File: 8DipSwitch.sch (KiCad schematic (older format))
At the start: 12 parts

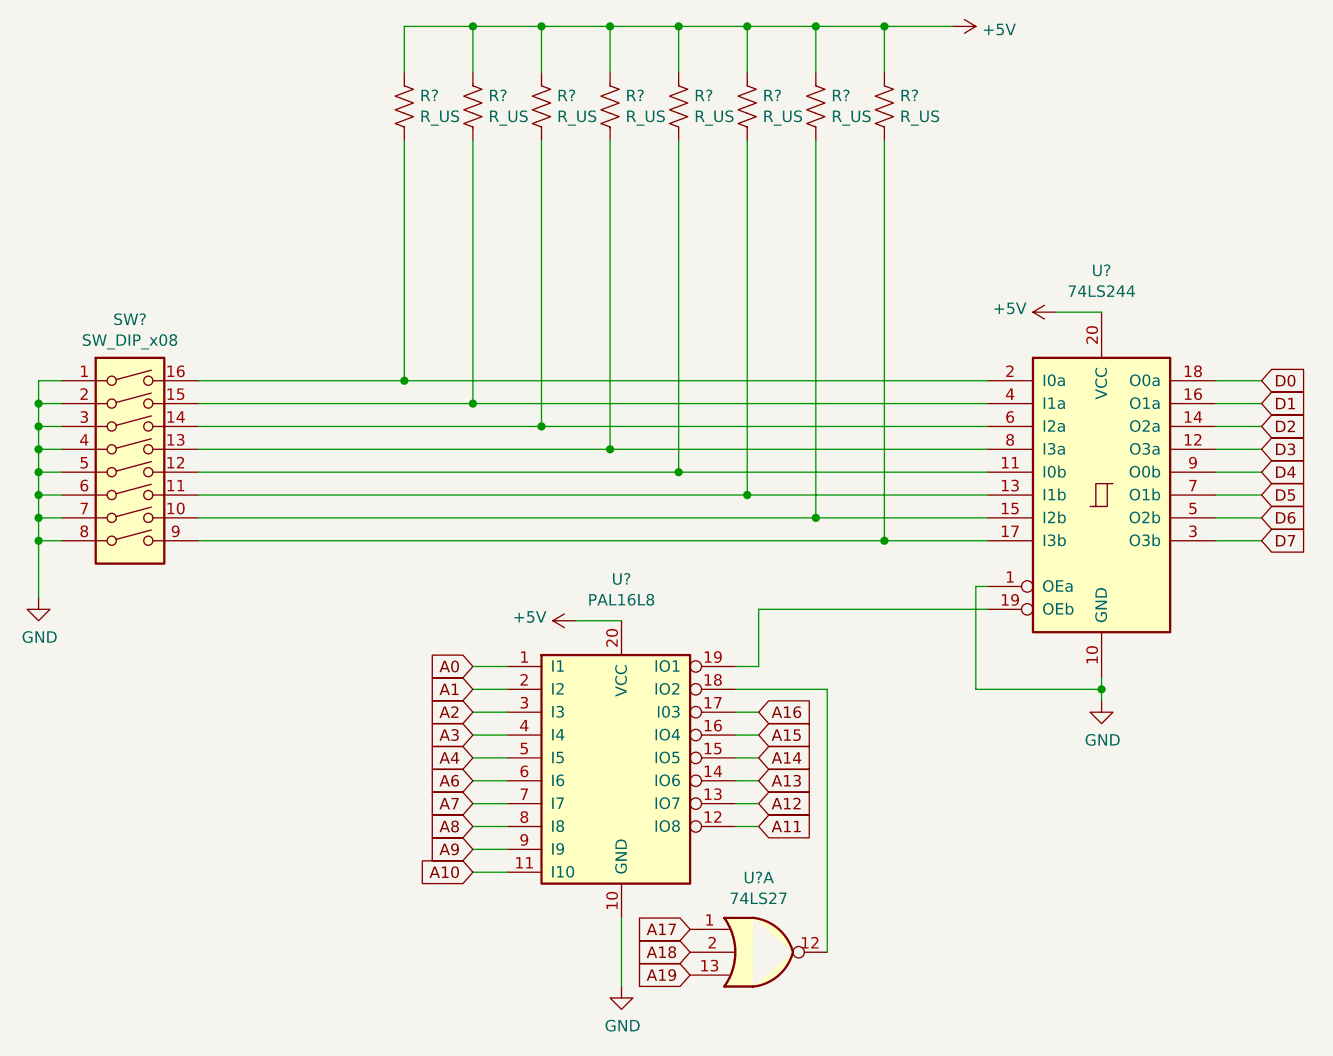
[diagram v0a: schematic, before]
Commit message: adjusted and incorperated 8dipswitch to pcb
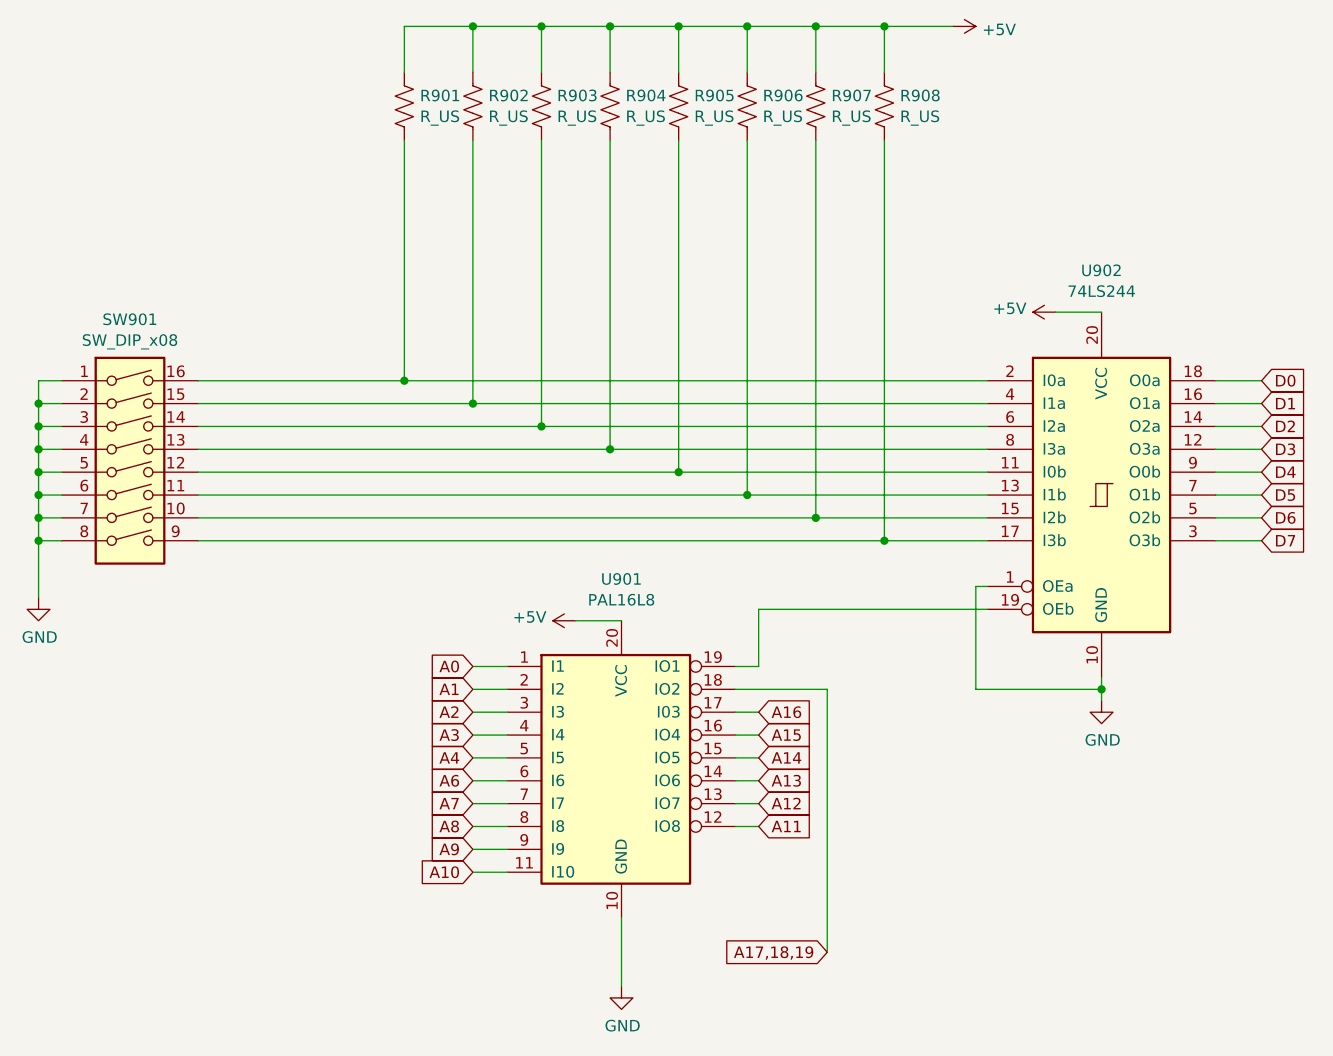
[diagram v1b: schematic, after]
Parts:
- removed U?: 74LS27, symbol 74xx:74LS27
- R901, R902, R903, R904, R905, R906, R907, R908: renamed from R?; footprint (none) -> Resistor_SMD:R_0805_2012Metric
- SW901: renamed from SW?; footprint (none) -> Button_Switch_SMD:SW_DIP_SPSTx08_Slide_6.7x21.88mm_W6.73mm_P2.54mm_LowProfile_JPin
- U901, U902: renamed from U?; footprint (none) -> Package_DIP:DIP-20_W7.62mm_SMDSocket_SmallPads
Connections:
- net A17,18,19: now reaches U901.18 (IO2)
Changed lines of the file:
@@
 $Descr A4 11693 8268
 encoding utf-8
-Sheet 3 3
+Sheet 9 9
 Title ""
 Date ""
@@
 $EndDescr
 $Comp
-L 74xx:74LS244 U?
+L 74xx:74LS244 U902
 U 1 1 60E9FDCB
 P 6150 3050
-F 0 "U?" H 6150 4031 50  0000 C CNN
+F 0 "U902" H 6150 4031 50  0000 C CNN
 F 1 "74LS244" H 6150 3940 50  0000 C CNN
-F 2 "" H 6150 3050 50  0001 C CNN
+F 2 "Package_DIP:DIP-20_W7.62mm_SMDSocket_SmallPads" H 6150 3050 50  0001 C CNN
 F 3 "http://www.ti.com/lit/ds/symlink/sn74ls244.pdf" H 6150 3050 50  0001 C CNN
 	1    6150 3050
@@
 $EndComp
 $Comp
-L Switch:SW_DIP_x08 SW?
+L Switch:SW_DIP_x08 SW901
 U 1 1 60EA4BCE
 P 1900 2950
-F 0 "SW?" H 1900 3617 50  0000 C CNN
+F 0 "SW901" H 1900 3617 50  0000 C CNN
 F 1 "SW_DIP_x08" H 1900 3526 50  0000 C CNN
-F 2 "" H 1900 2950 50  0001 C CNN
+F 2 "Button_Switch_SMD:SW_DIP_SPSTx08_Slide_6.7x21.88mm_W6.73mm_P2.54mm_LowProfile_JPin" H 1900 2950 50  0001 C CNN
 F 3 "~" H 1900 2950 50  0001 C CNN
 	1    1900 2950
@@
 	1500 3250 1500 3500
 $Comp
-L power:GND #PWR0117
+L power:GND #PWR0128
 U 1 1 60EA71D9
 P 1500 3500
-F 0 "#PWR0117" H 1500 3250 50  0001 C CNN
+F 0 "#PWR0128" H 1500 3250 50  0001 C CNN
 F 1 "GND" H 1505 3327 50  0000 C CNN
 F 2 "" H 1500 3500 50  0001 C CNN
@@
 $EndComp
 $Comp
-L Device:R_US R?
+L Device:R_US R901
 U 1 1 60EAB661
 P 3100 1350
-F 0 "R?" H 3168 1396 50  0000 L CNN
+F 0 "R901" H 3168 1396 50  0000 L CNN
 F 1 "R_US" H 3168 1305 50  0000 L CNN
-F 2 "" V 3140 1340 50  0001 C CNN
+F 2 "Resistor_SMD:R_0805_2012Metric" V 3140 1340 50  0001 C CNN
 F 3 "~" H 3100 1350 50  0001 C CNN
 	1    3100 1350
@@
 $EndComp
 $Comp
-L Device:R_US R?
+L Device:R_US R902
 U 1 1 60EACC67
 P 3400 1350
-F 0 "R?" H 3468 1396 50  0000 L CNN
+F 0 "R902" H 3468 1396 50  0000 L CNN
 F 1 "R_US" H 3468 1305 50  0000 L CNN
-F 2 "" V 3440 1340 50  0001 C CNN
+F 2 "Resistor_SMD:R_0805_2012Metric" V 3440 1340 50  0001 C CNN
 F 3 "~" H 3400 1350 50  0001 C CNN
 	1    3400 1350
@@
 $EndComp
 $Comp
-L Device:R_US R?
+L Device:R_US R903
 U 1 1 60EAD3B5
 P 3700 1350
-F 0 "R?" H 3768 1396 50  0000 L CNN
+F 0 "R903" H 3768 1396 50  0000 L CNN
 F 1 "R_US" H 3768 1305 50  0000 L CNN
-F 2 "" V 3740 1340 50  0001 C CNN
+F 2 "Resistor_SMD:R_0805_2012Metric" V 3740 1340 50  0001 C CNN
 F 3 "~" H 3700 1350 50  0001 C CNN
 	1    3700 1350
@@
 $EndComp
 $Comp
-L Device:R_US R?
+L Device:R_US R904
 U 1 1 60EADB2C
 P 4000 1350
-F 0 "R?" H 4068 1396 50  0000 L CNN
+F 0 "R904" H 4068 1396 50  0000 L CNN
 F 1 "R_US" H 4068 1305 50  0000 L CNN
-F 2 "" V 4040 1340 50  0001 C CNN
+F 2 "Resistor_SMD:R_0805_2012Metric" V 4040 1340 50  0001 C CNN
 F 3 "~" H 4000 1350 50  0001 C CNN
 	1    4000 1350
@@
 $EndComp
 $Comp
-L Device:R_US R?
+L Device:R_US R905
 U 1 1 60EADC9B
 P 4300 1350
-F 0 "R?" H 4368 1396 50  0000 L CNN
+F 0 "R905" H 4368 1396 50  0000 L CNN
 F 1 "R_US" H 4368 1305 50  0000 L CNN
-F 2 "" V 4340 1340 50  0001 C CNN
+F 2 "Resistor_SMD:R_0805_2012Metric" V 4340 1340 50  0001 C CNN
 F 3 "~" H 4300 1350 50  0001 C CNN
 	1    4300 1350
@@
 $EndComp
 $Comp
-L Device:R_US R?
+L Device:R_US R906
 U 1 1 60EADEEE
 P 4600 1350
-F 0 "R?" H 4668 1396 50  0000 L CNN
+F 0 "R906" H 4668 1396 50  0000 L CNN
 F 1 "R_US" H 4668 1305 50  0000 L CNN
-F 2 "" V 4640 1340 50  0001 C CNN
+F 2 "Resistor_SMD:R_0805_2012Metric" V 4640 1340 50  0001 C CNN
 F 3 "~" H 4600 1350 50  0001 C CNN
 	1    4600 1350
@@
 $EndComp
 $Comp
-L Device:R_US R?
+L Device:R_US R907
 U 1 1 60EB10EA
 P 4900 1350
-F 0 "R?" H 4968 1396 50  0000 L CNN
+F 0 "R907" H 4968 1396 50  0000 L CNN
 F 1 "R_US" H 4968 1305 50  0000 L CNN
-F 2 "" V 4940 1340 50  0001 C CNN
+F 2 "Resistor_SMD:R_0805_2012Metric" V 4940 1340 50  0001 C CNN
 F 3 "~" H 4900 1350 50  0001 C CNN
 	1    4900 1350
@@
 $EndComp
 $Comp
-L Device:R_US R?
+L Device:R_US R908
 U 1 1 60EB1338
 P 5200 1350
-F 0 "R?" H 5268 1396 50  0000 L CNN
+F 0 "R908" H 5268 1396 50  0000 L CNN
 F 1 "R_US" H 5268 1305 50  0000 L CNN
-F 2 "" V 5240 1340 50  0001 C CNN
+F 2 "Resistor_SMD:R_0805_2012Metric" V 5240 1340 50  0001 C CNN
 F 3 "~" H 5200 1350 50  0001 C CNN
 	1    5200 1350
@@
 	5200 3250 5650 3250
 $Comp
-L power:GND #PWR0118
+L power:GND #PWR0129
 U 1 1 60EC2703
 P 6150 3950
-F 0 "#PWR0118" H 6150 3700 50  0001 C CNN
+F 0 "#PWR0129" H 6150 3700 50  0001 C CNN
 F 1 "GND" H 6155 3777 50  0000 C CNN
 F 2 "" H 6150 3950 50  0001 C CNN
@@
 AR Path="/60860E4C/60BCFB6D" Ref="#PWR?"  Part="1"
 AR Path="/60E9DA87/60BCFB6D" Ref="#PWR0119"  Part="1"
-F 0 "#PWR0119" H 4050 4950 50  0001 C CNN
+AR Path="/60AD5691/60BCFB6D" Ref="#PWR0130"  Part="1"
+F 0 "#PWR0130" H 4050 4950 50  0001 C CNN
 F 1 "GND" H 4055 5027 50  0000 C CNN
 F 2 "" H 4050 5200 50  0001 C CNN
@@
 AR Path="/60860E4C/60BCFB88" Ref="U?"  Part="1"
 AR Path="/60E9DA87/60BCFB88" Ref="U?"  Part="1"
-F 0 "U?" H 4050 5181 50  0000 C CNN
+AR Path="/60AD5691/60BCFB88" Ref="U901"  Part="1"
+F 0 "U901" H 4050 5181 50  0000 C CNN
 F 1 "PAL16L8" H 4050 5090 50  0000 C CNN
-F 2 "" H 4050 4300 50  0001 C CNN
+F 2 "Package_DIP:DIP-20_W7.62mm_SMDSocket_SmallPads" H 4050 4300 50  0001 C CNN
 F 3 "" H 4050 4300 50  0001 C CNN
 	1    4050 4300
@@
 Wire Wire Line
 	4550 3900 4950 3900
-Text GLabel 4350 4950 0    50   Input ~ 0
-A17
-Text GLabel 4350 5150 0    50   Input ~ 0
-A19
 Wire Wire Line
 	5650 3550 4650 3550
@@
 D1
 $Comp
-L power:+5V #PWR0120
+L power:+5V #PWR0131
 U 1 1 60C1C4BE
 P 5950 2250
-F 0 "#PWR0120" H 5950 2100 50  0001 C CNN
+F 0 "#PWR0131" H 5950 2100 50  0001 C CNN
 F 1 "+5V" V 5965 2378 50  0000 L CNN
 F 2 "" H 5950 2250 50  0001 C CNN
@@
 $EndComp
 $Comp
-L power:+5V #PWR0121
+L power:+5V #PWR0132
 U 1 1 60C22353
 P 5500 1000
-F 0 "#PWR0121" H 5500 850 50  0001 C CNN
+F 0 "#PWR0132" H 5500 850 50  0001 C CNN
 F 1 "+5V" V 5515 1128 50  0000 L CNN
 F 2 "" H 5500 1000 50  0001 C CNN
@@
 $EndComp
 $Comp
-L power:+5V #PWR0122
+L power:+5V #PWR0133
 U 1 1 60C26D46
 P 3850 3600
-F 0 "#PWR0122" H 3850 3450 50  0001 C CNN
+F 0 "#PWR0133" H 3850 3450 50  0001 C CNN
 F 1 "+5V" V 3865 3728 50  0000 L CNN
 F 2 "" H 3850 3600 50  0001 C CNN
@@
 Text GLabel 3400 4200 0    50   Input ~ 0
 A4
-Text GLabel 4350 5050 0    50   Input ~ 0
-A18
-$Comp
-L 74xx:74LS27 U?
-U 1 1 60CA40E2
-P 4650 5050
-F 0 "U?" H 4650 5375 50  0000 C CNN
-F 1 "74LS27" H 4650 5284 50  0000 C CNN
-F 2 "" H 4650 5050 50  0001 C CNN
-F 3 "http://www.ti.com/lit/gpn/sn74LS27" H 4650 5050 50  0001 C CNN
-	1    4650 5050
-	1    0    0    -1
-$EndComp
+Text GLabel 4950 5050 0    50   Input ~ 0
+A17,18,19
 $EndSCHEMATC
